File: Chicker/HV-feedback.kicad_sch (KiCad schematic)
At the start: 10 parts, among them U8 MCP6231UT-E/OT

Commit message: chicker modifications (mostly ready to order)
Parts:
- removed D20: NZ9F3V3T5G, bots:SOD-923, symbol thebots_symlib:D_ZENER_NZ9F3V3T5G
- added D20: BZT52C3V3T-7, bots:D_SOD-523, symbol thebots_symlib:D_ZENER_BZT52C3V3T-7
- U8: footprint bots:SOT-23-5 -> Package_TO_SOT_SMD:SOT-23-5; LCSC C22795 -> C412821; MPN MCP6231UT-E/OT -> MCP6001UT-E/OT
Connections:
- net GND: now also D20.2 (A)
- net HV_SENSE: now also D20.1 (K)

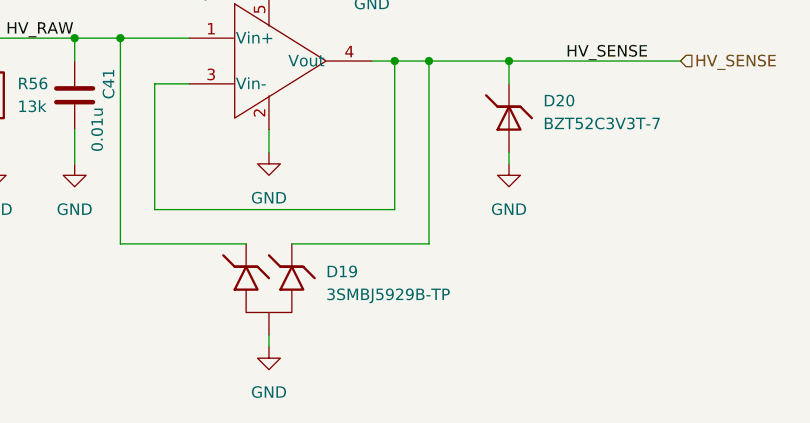
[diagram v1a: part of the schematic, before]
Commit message: fixed most issues with JLC ordering
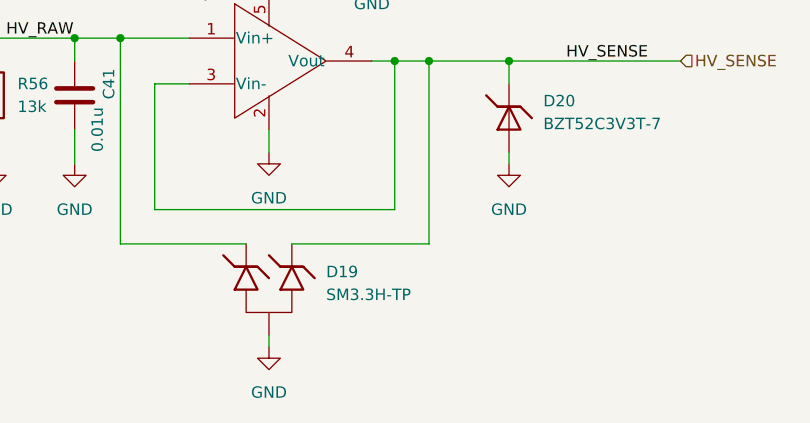
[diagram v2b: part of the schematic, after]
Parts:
- D19: value 3SMBJ5929B-TP -> SM3.3H-TP; footprint bots:SOT-23 -> Package_TO_SOT_SMD:SOT-23; MPN 3SMBJ5929B-TP -> SM3.3H-TP
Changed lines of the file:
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@@
+	)
+	(symbol
+		(lib_id "thebots_symlib:D_TVS_FSM3.3H-TP")
+		(at 91.44 82.55 270)
+		(unit 1)
+		(exclude_from_sim no)
+		(in_bom yes)
+		(on_board yes)
+		(dnp no)
+		(fields_autoplaced yes)
+		(property "Reference" "D19"
+			(at 97.79 81.8514 90)
+			(effects
+				(font
+					(size 1.27 1.27)
+				)
+				(justify left)
+			)
+		)
+		(property "Value" "SM3.3H-TP"
+			(at 97.79 84.3914 90)
+			(effects
+				(font
+					(size 1.27 1.27)
+				)
+				(justify left)
+			)
+		)
+		(property "Footprint" "Package_TO_SOT_SMD:SOT-23"
+			(at 85.09 86.36 0)
+			(effects
+				(font
+					(size 1.27 1.27)
+				)
+				(hide yes)
+			)
+		)
+		(property "Datasheet" "~"
+			(at 86.36 85.09 0)
+			(effects
+				(font
+					(size 1.27 1.27)
+				)
+				(hide yes)
+			)
+		)
+		(property "Description" "Zener diode"
+			(at 91.44 82.55 0)
+			(effects
+				(font
+					(size 1.27 1.27)
+				)
+				(hide yes)
+			)
+		)
+		(property "MPN" "SM3.3H-TP"
+			(at 85.09 86.36 0)
+			(effects
+				(font
+					(size 1.27 1.27)
+				)
+				(hide yes)
+			)
+		)
+		(property "Manufacturer" "Micro Commercial Co"
+			(at 86.36 85.09 0)
+			(effects
+				(font
+					(size 1.27 1.27)
+				)
+				(hide yes)
+			)
+		)
+		(property "Price" "0.63"
+			(at 86.36 85.09 0)
+			(effects
+				(font
+					(size 1.27 1.27)
+				)
+				(hide yes)
+			)
+		)
+		(property "JLC" ""
+			(at 88.9 82.55 0)
+			(effects
+				(font
+					(size 1.27 1.27)
+				)
+				(hide yes)
+			)
+		)
+		(property "LCSC" "N/A"
+			(at 86.36 85.09 0)
+			(effects
+				(font
+					(size 1.27 1.27)
+				)
+				(hide yes)
+			)
+		)
+		(pin "2"
+		)
+		(pin "1"
+		)
+		(pin "3"
+		)
+		(instances
+			(project "chicker"
+				(path "/1a9ce3e8-a091-496c-9c5f-e7b2eb60e275/ec2690de-9d43-42f0-9a1d-89d3edcde356"
+					(reference "D19")
+					(unit 1)
+				)
+			)
+		)
 	)
 	(symbol
@@
 					(unit 1)
 				)
-			)
-		)
-	)
-	(symbol
-		(lib_id "thebots_symlib:D_TVS_FSM3.3H-TP")
-		(at 91.44 82.55 270)
-		(unit 1)
-		(exclude_from_sim no)
-		(in_bom yes)
-		(on_board yes)
-		(dnp no)
-		(fields_autoplaced yes)
-		(property "Reference" "D19"
-			(at 97.79 81.8515 90)
-			(effects
-				(font
-					(size 1.27 1.27)
-				)
-				(justify left)
-			)
-		)
-		(property "Value" "3SMBJ5929B-TP\n"
-			(at 97.79 84.3915 90)
-			(effects
-				(font
-					(size 1.27 1.27)
-				)
-				(justify left)
-			)
-		)
-		(property "Footprint" "bots:SOT-23"
-			(at 85.09 86.36 0)
-			(effects
-				(font
-					(size 1.27 1.27)
-				)
-				(hide yes)
-			)
-		)
-		(property "Datasheet" "~"
-			(at 86.36 85.09 0)
-			(effects
-				(font
-					(size 1.27 1.27)
-				)
-				(hide yes)
-			)
-		)
-		(property "Description" ""
-			(at 91.44 82.55 0)
-			(effects
-				(font
-					(size 1.27 1.27)
-				)
-				(hide yes)
-			)
-		)
-		(property "MPN" "3SMBJ5929B-TP"
-			(at 85.09 86.36 0)
-			(effects
-				(font
-					(size 1.27 1.27)
-				)
-				(hide yes)
-			)
-		)
-		(property "Manufacturer" "Micro Commercial Co"
-			(at 86.36 85.09 0)
-			(effects
-				(font
-					(size 1.27 1.27)
-				)
-				(hide yes)
-			)
-		)
-		(property "Price" "0.63"
-			(at 86.36 85.09 0)
-			(effects
-				(font
-					(size 1.27 1.27)
-				)
-				(hide yes)
-			)
-		)
-		(property "JLC" ""
-			(at 88.9 82.55 0)
-			(effects
-				(font
-					(size 1.27 1.27)
-				)
-				(hide yes)
-			)
-		)
-		(property "LCSC" "N/A"
-			(at 86.36 85.09 0)
-			(effects
-				(font
-					(size 1.27 1.27)
-				)
-				(hide yes)
-			)
-		)
-		(pin "1"
-		)
-		(pin "2"
-		)
-		(pin "3"
-		)
-		(instances
-			(project "chicker"
-				(path "/1a9ce3e8-a091-496c-9c5f-e7b2eb60e275/ec2690de-9d43-42f0-9a1d-89d3edcde356"
-					(reference "D19")
-					(unit 1)
-				)

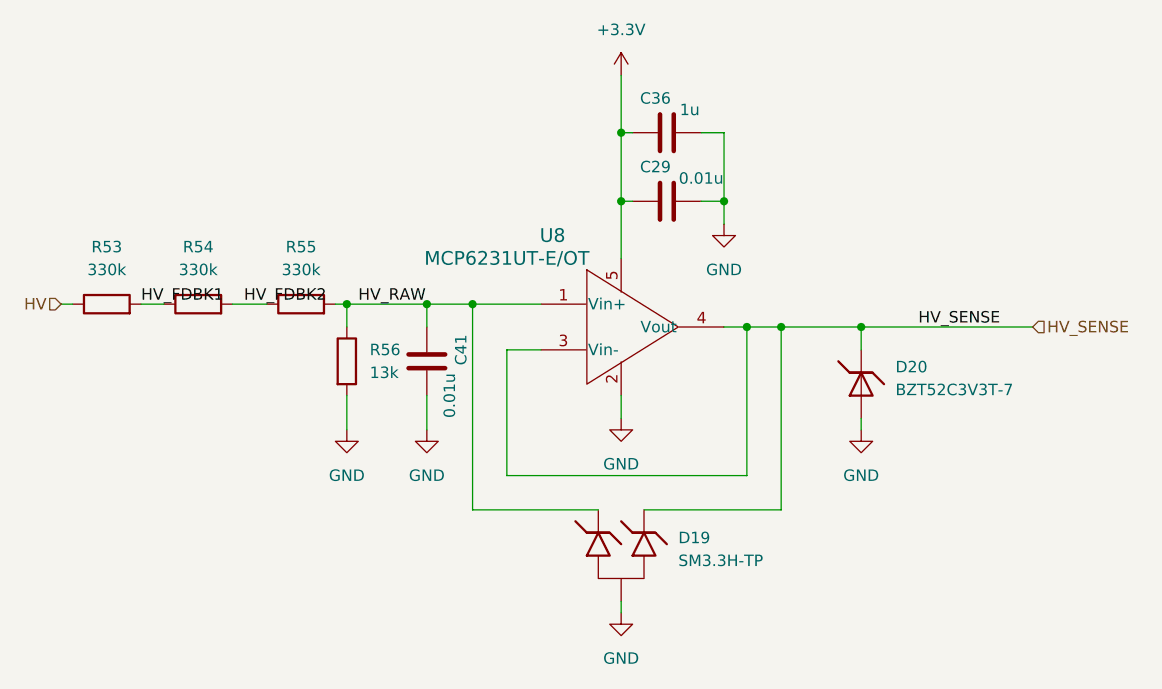
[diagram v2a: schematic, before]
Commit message: ESD+schematic fixes
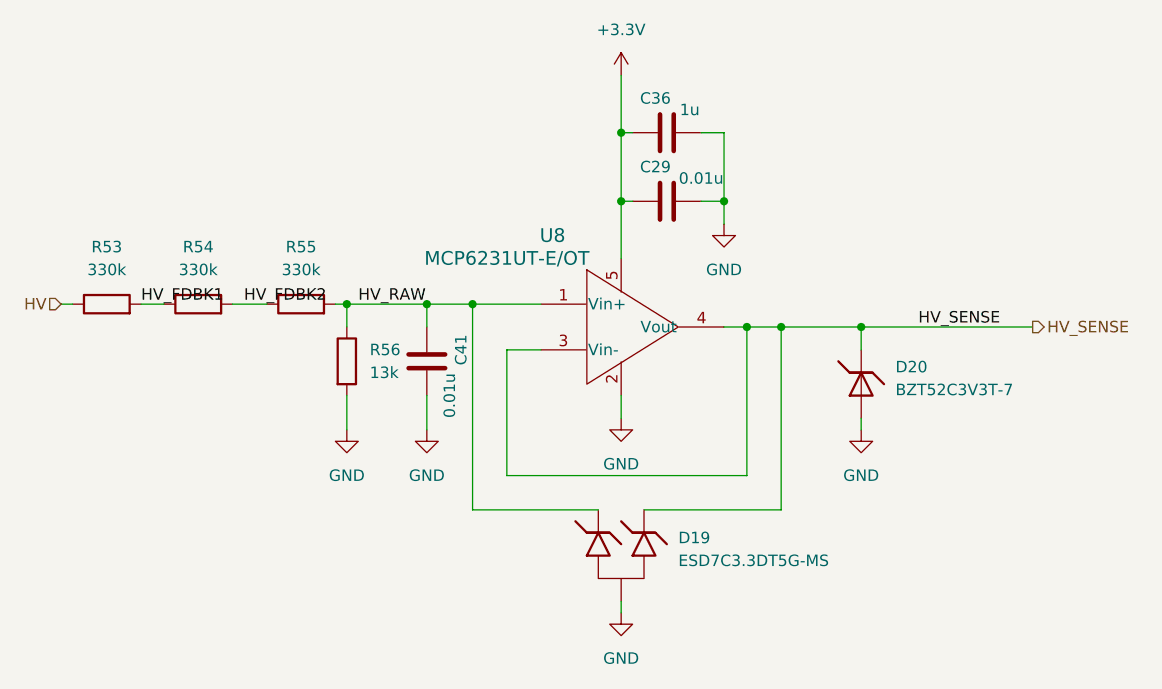
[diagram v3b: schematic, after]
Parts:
- removed D19: SM3.3H-TP, Package_TO_SOT_SMD:SOT-23, symbol thebots_symlib:D_TVS_FSM3.3H-TP
- added D19: ESD7C3.3DT5G-MS, bots:SOT-723, symbol bots:D_TVS_ESD
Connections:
- net GND: now also D19.3
- net HV_RAW: now also D19.2
- net HV_SENSE: now also D19.1
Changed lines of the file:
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@@
 (kicad_sch
-	(version 20231120)
+	(version 20250114)
 	(generator "eeschema")
-	(generator_version "8.0")
+	(generator_version "9.0")
 	(paper "A5")
 	(junction
@@
 	(label "HV_RAW"
 		(at 62.23 55.88 0)
-		(fields_autoplaced yes)
 		(effects
 			(font
@@
 	(label "HV_FDBK1"
 		(at 38.1 55.88 0)
-		(fields_autoplaced yes)
 		(effects
 			(font
@@
 	(label "HV_SENSE"
 		(at 124.46 58.42 0)
-		(fields_autoplaced yes)
 		(effects
 			(font
@@
 	(label "HV_FDBK2"
 		(at 49.53 55.88 0)
-		(fields_autoplaced yes)
 		(effects
 			(font
@@
 	)
 	(hierarchical_label "HV_SENSE"
-		(shape input)
+		(shape output)
 		(at 137.16 58.42 0)
-		(fields_autoplaced yes)
 		(effects
 			(font
@@
 		(shape input)
 		(at 29.21 55.88 180)
-		(fields_autoplaced yes)
 		(effects
 			(font
@@
 	)
 	(symbol
+		(lib_id "bots:D_TVS_ESD")
+		(at 91.44 82.55 270)
+		(unit 1)
+		(exclude_from_sim no)
+		(in_bom yes)
+		(on_board yes)
+		(dnp no)
+		(fields_autoplaced yes)
+		(property "Reference" "D19"
+			(at 97.79 81.8514 90)
+			(effects
+				(font
+					(size 1.27 1.27)
+				)
+				(justify left)
+			)
+		)
+		(property "Value" "ESD7C3.3DT5G-MS"
+			(at 97.79 84.3914 90)
+			(effects
+				(font
+					(size 1.27 1.27)
+				)
+				(justify left)
+			)
+		)
+		(property "Footprint" "bots:SOT-723"
+			(at 85.09 86.36 0)
+			(effects
+				(font
+					(size 1.27 1.27)
+				)
+				(hide yes)
+			)
+		)
+		(property "Datasheet" "~"
+			(at 86.36 85.09 0)
+			(effects
+				(font
+					(size 1.27 1.27)
+				)
+				(hide yes)
+			)
+		)
+		(property "Description" "Zener diode"
+			(at 91.44 82.55 0)
+			(effects
+				(font
+					(size 1.27 1.27)
+				)
+				(hide yes)
+			)
+		)
+		(property "MPN" "ESD7C3.3DT5G-MS "
+			(at 85.09 86.36 0)
+			(effects
+				(font
+					(size 1.27 1.27)
+				)
+				(hide yes)
+			)
+		)
+		(property "Manufacturer" "Micro Commercial Co"
+			(at 86.36 85.09 0)
+			(effects
+				(font
+					(size 1.27 1.27)
+				)
+				(hide yes)
+			)
+		)
+		(property "Price" "0.63"
+			(at 86.36 85.09 0)
+			(effects
+				(font
+					(size 1.27 1.27)
+				)
+				(hide yes)
+			)
+		)
+		(property "JLC" "C5331072"
+			(at 88.9 82.55 0)
+			(effects
+				(font
+					(size 1.27 1.27)
+				)
+				(hide yes)
+			)
+		)
+		(property "LCSC" "N/A"
+			(at 86.36 85.09 0)
+			(effects
+				(font
+					(size 1.27 1.27)
+				)
+				(hide yes)
+			)
+		)
+		(property "extended" "no"
+			(at 91.44 82.55 0)
+			(effects
+				(font
+					(size 1.27 1.27)
+				)
+				(hide yes)
+			)
+		)
+		(pin "2"
+		)
+		(pin "3"
+		)
+		(pin "1"
+		)
+		(instances
+			(project ""
+				(path "/1a9ce3e8-a091-496c-9c5f-e7b2eb60e275/ec2690de-9d43-42f0-9a1d-89d3edcde356"
+					(reference "D19")
+					(unit 1)
+				)
+			)
+		)
+	)
+	(symbol
 		(lib_id "power:GND")
 		(at 69.85 69.85 0)
@@
 					(unit 1)
 				)
-			)
-		)
-	)
-	(symbol
-		(lib_id "thebots_symlib:D_TVS_FSM3.3H-TP")
-		(at 91.44 82.55 270)
-		(unit 1)
-		(exclude_from_sim no)
-		(in_bom yes)
-		(on_board yes)
-		(dnp no)
-		(fields_autoplaced yes)
-		(property "Reference" "D19"
-			(at 97.79 81.8514 90)
-			(effects
-				(font
-					(size 1.27 1.27)
-				)
-				(justify left)
-			)
-		)
-		(property "Value" "SM3.3H-TP"
-			(at 97.79 84.3914 90)
-			(effects
-				(font
-					(size 1.27 1.27)
-				)
-				(justify left)
-			)
-		)
-		(property "Footprint" "Package_TO_SOT_SMD:SOT-23"
-			(at 85.09 86.36 0)
-			(effects
-				(font
-					(size 1.27 1.27)
-				)
-				(hide yes)
-			)
-		)
-		(property "Datasheet" "~"
-			(at 86.36 85.09 0)
-			(effects
-				(font
-					(size 1.27 1.27)
-				)
-				(hide yes)
-			)
-		)
-		(property "Description" "Zener diode"
-			(at 91.44 82.55 0)
-			(effects
-				(font
-					(size 1.27 1.27)
-				)
-				(hide yes)
-			)
-		)
-		(property "MPN" "SM3.3H-TP"
-			(at 85.09 86.36 0)
-			(effects
-				(font
-					(size 1.27 1.27)
-				)
-				(hide yes)
-			)
-		)
-		(property "Manufacturer" "Micro Commercial Co"
-			(at 86.36 85.09 0)
-			(effects
-				(font
-					(size 1.27 1.27)
-				)
-				(hide yes)
-			)
-		)
-		(property "Price" "0.63"
-			(at 86.36 85.09 0)
-			(effects
-				(font
-					(size 1.27 1.27)
-				)
-				(hide yes)
-			)
-		)
-		(property "JLC" ""
-			(at 88.9 82.55 0)
-			(effects
-				(font
-					(size 1.27 1.27)
-				)
-				(hide yes)
-			)
-		)
-		(property "LCSC" "N/A"
-			(at 86.36 85.09 0)
-			(effects
-				(font
-					(size 1.27 1.27)
-				)
-				(hide yes)
-			)
-		)
-		(pin "2"
-		)
-		(pin "1"
-		)
-		(pin "3"
-		)
-		(instances
-			(project "chicker"
-				(path "/1a9ce3e8-a091-496c-9c5f-e7b2eb60e275/ec2690de-9d43-42f0-9a1d-89d3edcde356"
-					(reference "D19")
-					(unit 1)
-				)

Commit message: chicker v1.1 basic parts
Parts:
- removed D20: BZT52C3V3T-7, bots:D_SOD-523, symbol thebots_symlib:D_ZENER_BZT52C3V3T-7
- removed U8: MCP6231UT-E/OT, Package_TO_SOT_SMD:SOT-23-5, symbol thebots_symlib:MCP6231UT-E/OT
- added D20: BZT52C3V3T-7, bots:D_SOD-523, symbol bots:D_ZENER_BZT52C3V3T-7_alternate
- added U8: AMP_MCP6231UT_alternate, bots:SOT-23-5, symbol bots:AMP_MCP6231UT_alternate
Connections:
- net +3.3V: now also U8.5
- net GND: now also D20.2 (A), U8.2
- net HV_RAW: now also U8.1 (Vin+)
- net HV_SENSE: now also D20.1 (K), U8.3 (Vin-), U8.4 (Vout)

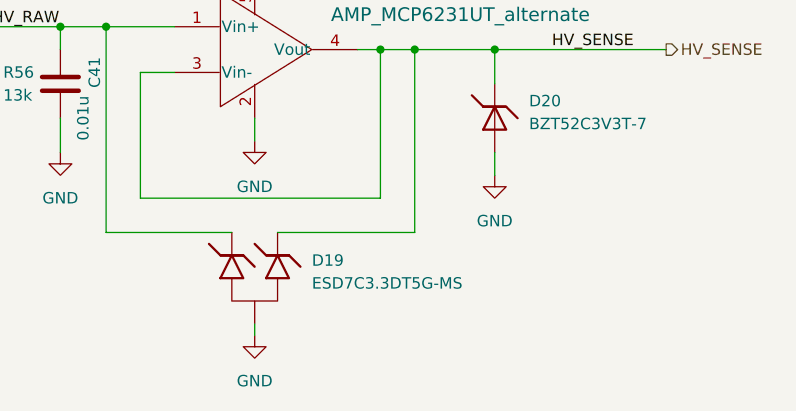
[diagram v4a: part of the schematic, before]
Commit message: changed more to basic
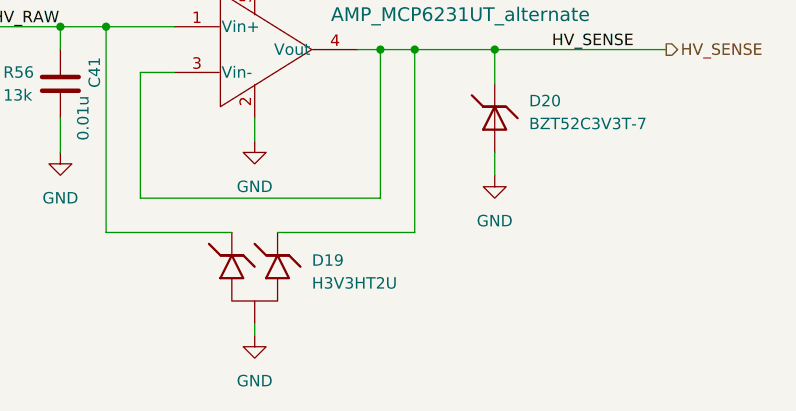
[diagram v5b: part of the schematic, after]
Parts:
- D19: value ESD7C3.3DT5G-MS -> H3V3HT2U; JLC C5331072 -> SOT-23; LCSC N/A -> C20617924; MPN ESD7C3.3DT5G-MS -> H3V3HT2U; Manufacturer Micro Commercial Co -> hongjiacheng; Price 0.63 -> 0.0379
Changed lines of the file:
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@@
 			)
 		)
-		(property "Value" "ESD7C3.3DT5G-MS"
+		(property "Value" "H3V3HT2U"
 			(at 97.79 84.3914 90)
 			(effects
@@
 			)
 		)
-		(property "Description" "Zener diode"
+		(property "Description" "Zener diode ESD"
 			(at 91.44 82.55 0)
 			(effects
@@
 			)
 		)
-		(property "MPN" "ESD7C3.3DT5G-MS "
+		(property "MPN" "H3V3HT2U"
 			(at 85.09 86.36 0)
 			(effects
@@
 			)
 		)
-		(property "Manufacturer" "Micro Commercial Co"
+		(property "Manufacturer" "hongjiacheng"
 			(at 86.36 85.09 0)
 			(effects
@@
 			)
 		)
-		(property "Price" "0.63"
+		(property "Price" "0.0379"
 			(at 86.36 85.09 0)
 			(effects
@@
 			)
 		)
-		(property "JLC" "C5331072"
+		(property "JLC" "SOT-23"
 			(at 88.9 82.55 0)
 			(effects
@@
 			)
 		)
-		(property "LCSC" "N/A"
+		(property "LCSC" "C20617924 "
 			(at 86.36 85.09 0)
 			(effects

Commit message: chicker v1.1 ordered!
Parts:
- D19: footprint bots:SOT-723 -> bots:SOT-23
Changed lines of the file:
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@@
 			)
 		)
-		(property "Footprint" "bots:SOT-723"
+		(property "Footprint" "bots:SOT-23"
 			(at 85.09 86.36 0)
 			(effects
